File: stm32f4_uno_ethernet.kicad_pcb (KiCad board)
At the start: 2 copper layers, 68.6 x 53.3 mm, 57 parts, among them J104 STM32 GPIO, J106 Power, J107 Ethernet, J110 Analog, J111 Conn_01x04, J201 RJ45-TH_B-1-1, U201 SRV05-4, U202 LAN8742A, Y201 25MHz

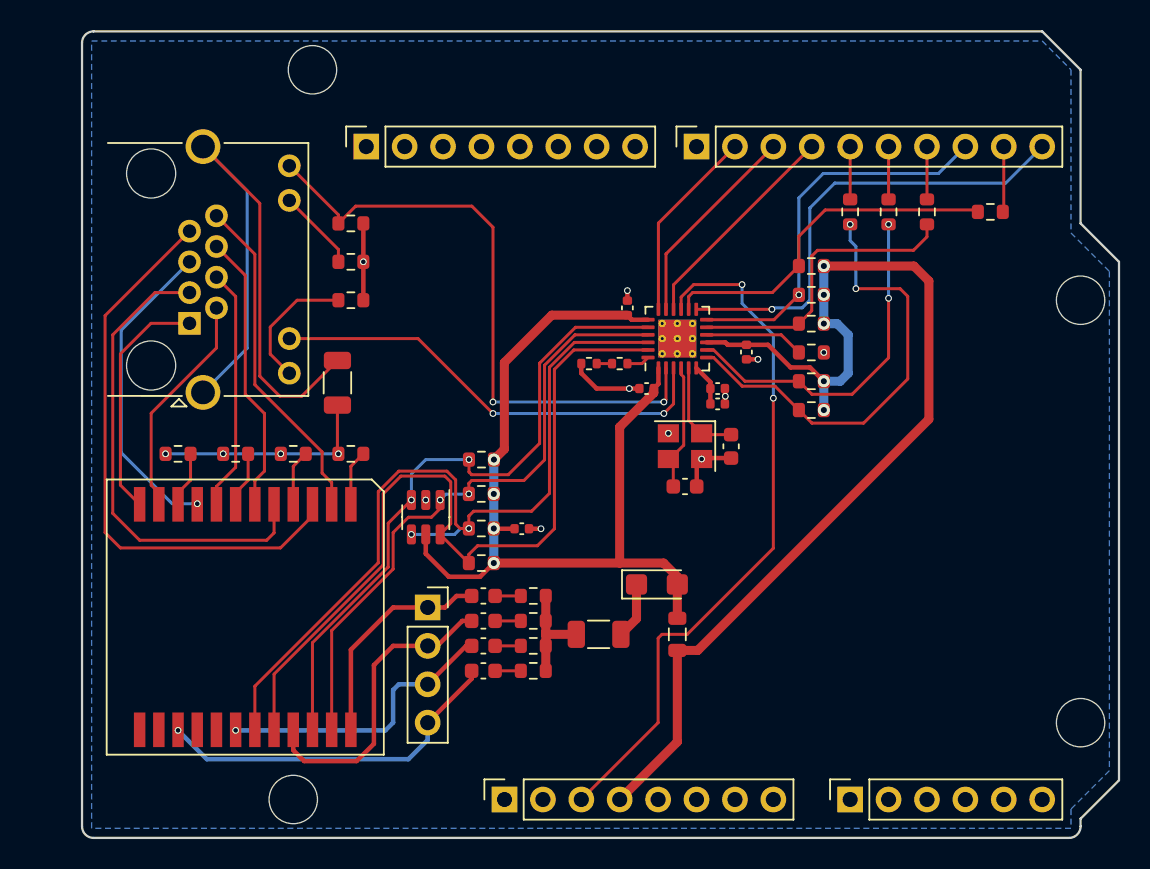
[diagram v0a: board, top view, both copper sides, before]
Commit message: Replace transformer, replace RJ45 3D model
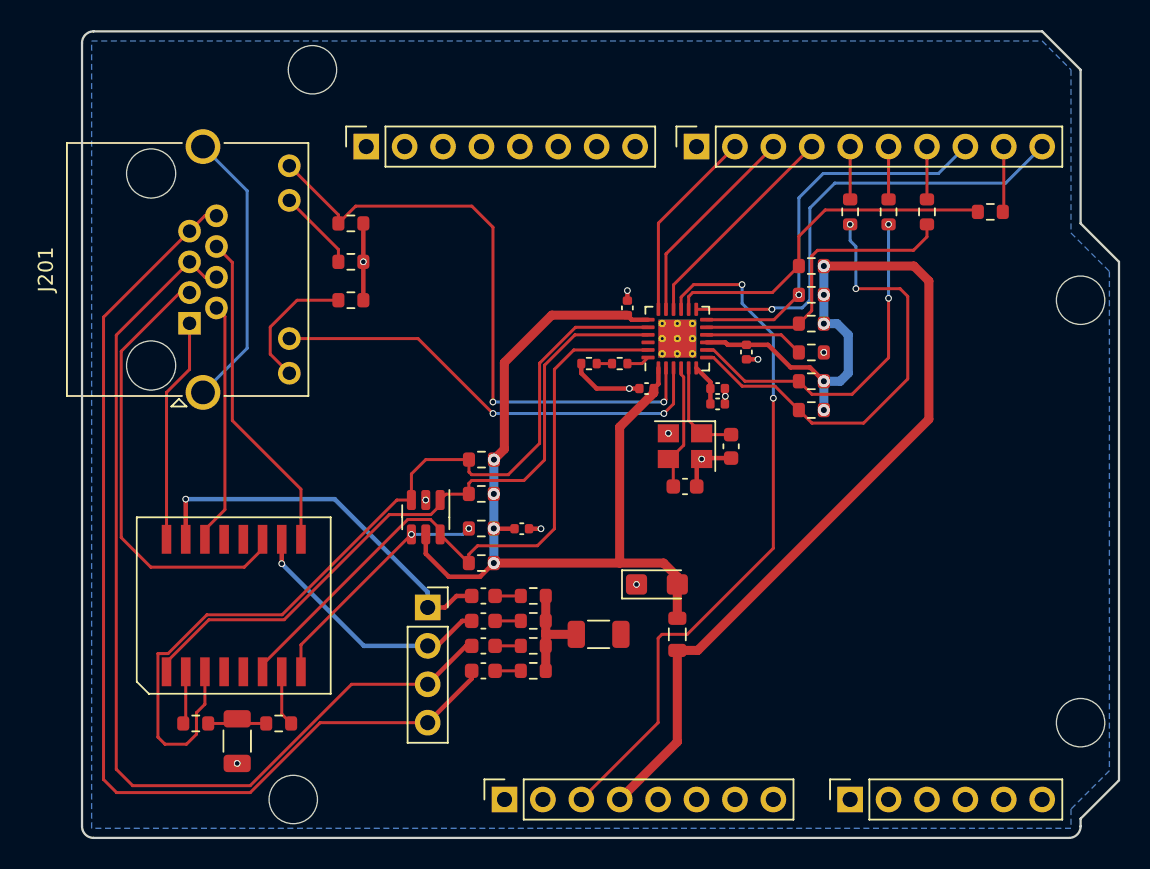
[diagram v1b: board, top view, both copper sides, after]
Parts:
- removed R218, R221: 75, Resistor_SMD:R_0603_1608Metric
- J201: footprint Project_Library:RJ45-TH_B-1-1 -> Project_Library:Boomele RJ45-TH_B-1-1
- TR201: value G2474CG -> YDS-Tech 11FB-05NL; footprint Project_Library:Mentech G2474CG 24pin 17.2mmx13.97mm -> Project_Library:YDS-Tech 11FB-05NL
- moved C208 24.6 mm to (110.3, 93.6), turned to -90 degrees
- moved R205 20.6 mm to (107.5, 92.4), turned to 180 degrees
- moved R213 17.9 mm to (113.0, 92.4)
- moved TR201 10.2 mm to (110.0, 84.6), turned to 0 degrees
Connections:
- C208 pad 2: Earth -> GND
- C213 pad 1: /Ethernet/PR45 -> /Ethernet/LAN4
- C214 pad 1: /Ethernet/PR78 -> /Ethernet/LAN7
- C215 pad 2: GND -> Earth
- J111 pad 3: /Ethernet/PR45 -> /Ethernet/LAN4
- J111 pad 4: /Ethernet/PR78 -> /Ethernet/LAN7
- J201 pad 5: /Ethernet/LAN5 -> /Ethernet/LAN4
- J201 pad 8: /Ethernet/LAN8 -> /Ethernet/LAN7
- R205 pad 2: Net-(R205-Pad2) -> Net-(TR201-C_TX)
- R213 pad 2: Net-(R213-Pad2) -> Net-(TR201-C_RX)
- TR201 pad 1: Net-(R205-Pad2) -> /Ethernet/TX+
- TR201 pad 10: Net-(R221-Pad2) -> /Ethernet/PR36
- TR201 pad 11: /Ethernet/LAN2 -> /Ethernet/LAN3
- TR201 pad 12: /Ethernet/LAN1 -> unconnected-(TR201-NC-Pad12)
- TR201 pad 14: unconnected-(TR201-MX4+-Pad14) -> /Ethernet/LAN2
- TR201 pad 15: /Ethernet/PR78 -> /Ethernet/PR12
- TR201 pad 16: unconnected-(TR201-MX3--Pad16) -> /Ethernet/LAN1
- TR201 pad 2: /Ethernet/LAN8 -> Net-(TR201-C_TX)
- TR201 pad 3: /Ethernet/LAN7 -> /Ethernet/TX-
- TR201 pad 4: Net-(R213-Pad2) -> unconnected-(TR201-NC-Pad4)
- TR201 pad 5: /Ethernet/LAN3 -> unconnected-(TR201-NC-Pad5)
- TR201 pad 6: /Ethernet/LAN6 -> /Ethernet/RX+
- TR201 pad 7: Net-(R218-Pad2) -> Net-(TR201-C_RX)
- TR201 pad 8: /Ethernet/LAN4 -> /Ethernet/RX-
- TR201 pad 9: /Ethernet/LAN5 -> /Ethernet/LAN6
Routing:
- net /Ethernet/LAN4: track 16.1 -> 65.5 mm
- net /Ethernet/RX-: track 55.2 -> 16.1 mm
- net /Ethernet/LAN7: track 38.0 -> 69.2 mm
- net /Ethernet/PR78: track 23.6 -> 0.00 mm, vias 1 -> 0
- net Earth: track 42.1 -> 18.7 mm
- net /Ethernet/LAN8: track 22.2 -> 0.00 mm
- net /Ethernet/LAN5: track 21.0 -> 0.00 mm, vias 1 -> 0
- net /Ethernet/PR45: track 19.2 -> 0.00 mm, vias 1 -> 0
- net /Ethernet/TX-: track 43.7 -> 59.7 mm, vias 2 -> 0
- net /Ethernet/PR12: track 14.8 -> 25.4 mm, vias 0 -> 1
- net /Ethernet/RX+: track 54.6 -> 44.0 mm
- net Net-(C208-Pad1): track 14.7 -> 4.09 mm, vias 4 -> 0
- net /Ethernet/TX+: track 41.4 -> 45.7 mm, vias 2 -> 0
- net GND: track 20.9 -> 17.2 mm, vias 10 -> 12
- net Net-(R221-Pad2): track 3.68 -> 0.00 mm
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
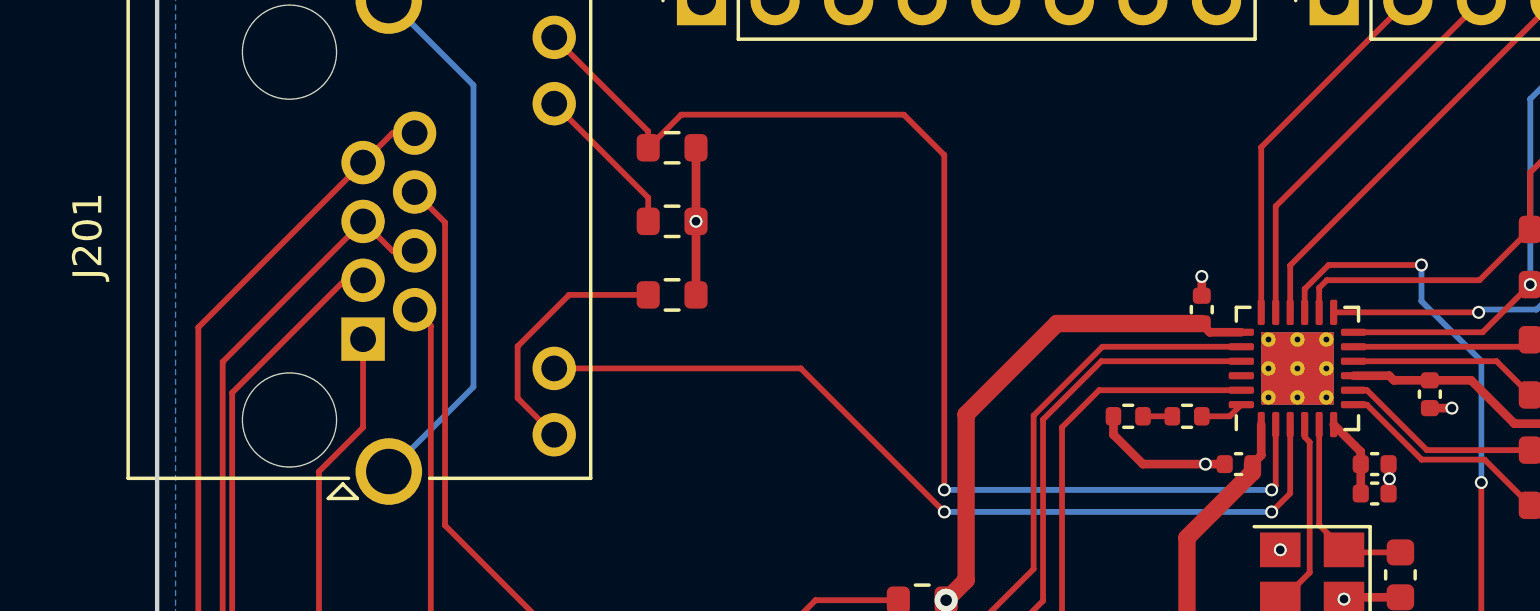
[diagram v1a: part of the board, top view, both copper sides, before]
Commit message: Change LAN footprint
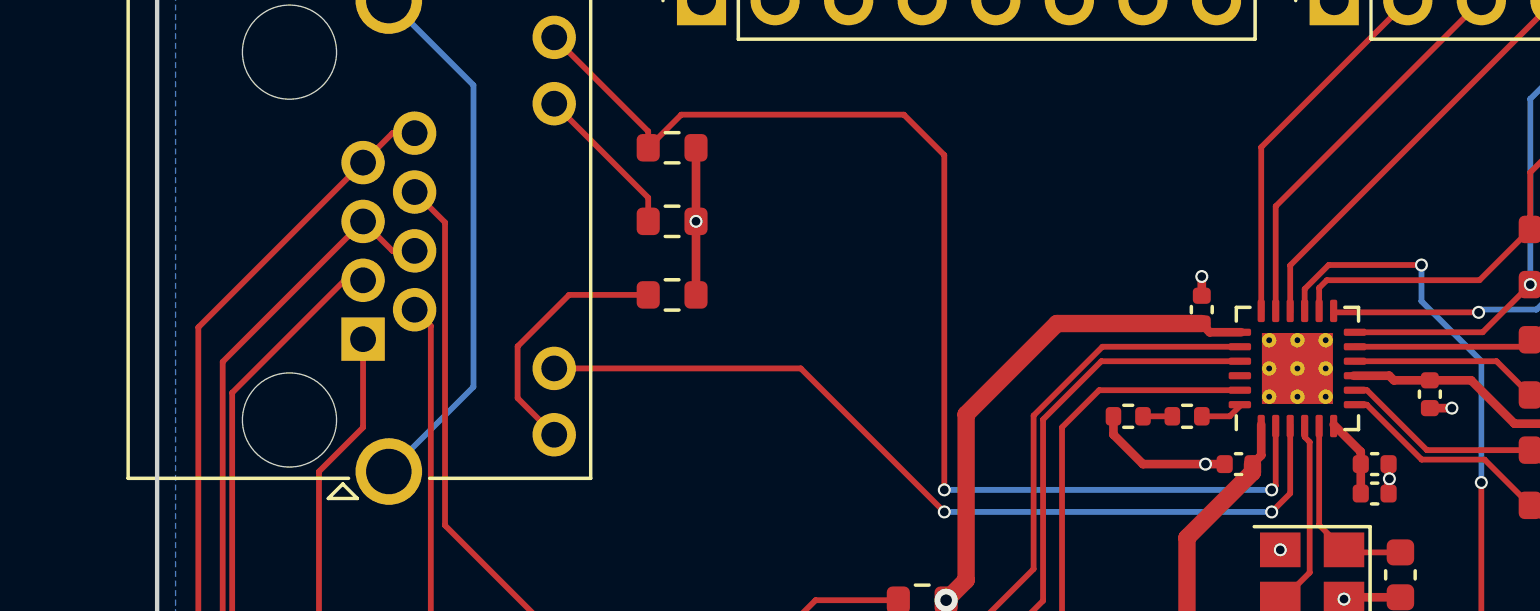
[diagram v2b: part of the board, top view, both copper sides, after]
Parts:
- U202: footprint Package_DFN_QFN:VQFN-24-1EP_4x4mm_P0.5mm_EP2.5x2.5mm_ThermalVias -> Package_DFN_QFN:VQFN-24-1EP_4x4mm_P0.5mm_EP2.45x2.45mm_ThermalVias

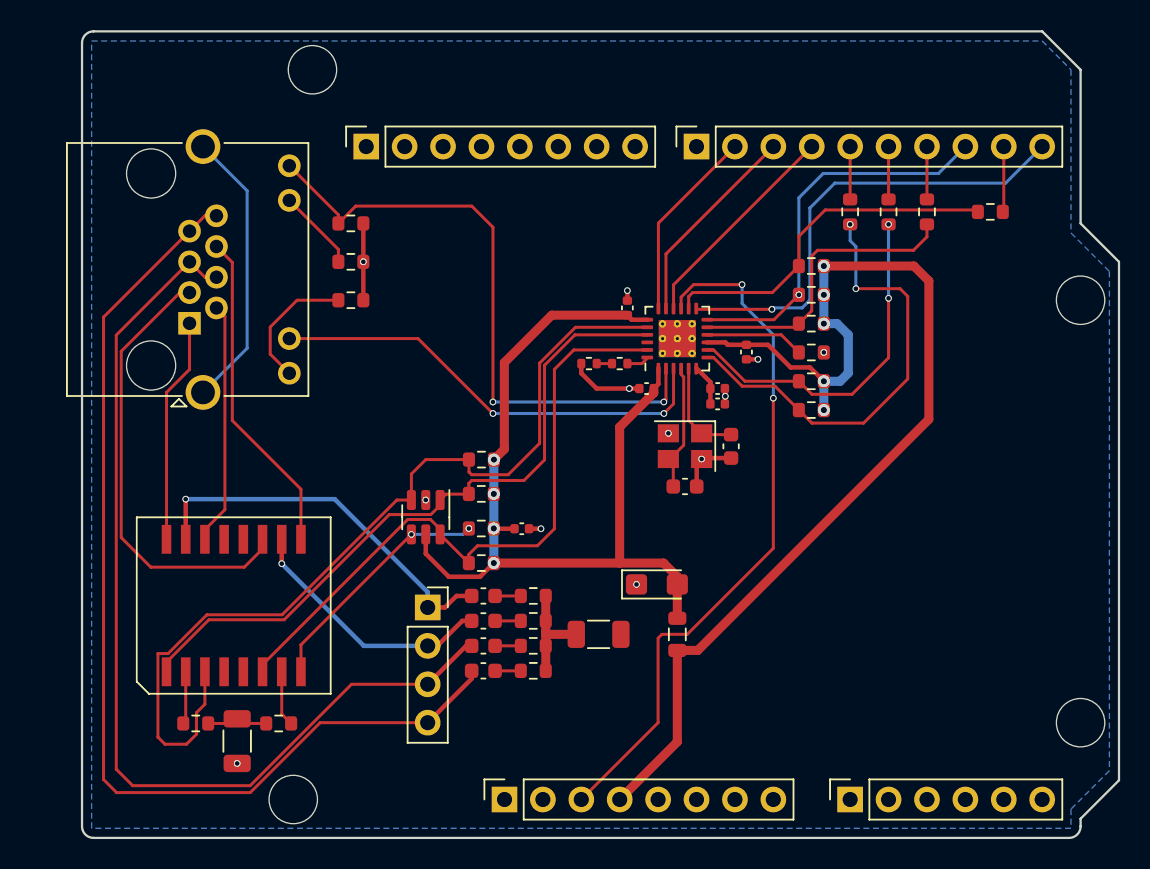
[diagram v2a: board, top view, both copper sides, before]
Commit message: Add ETH_RXER
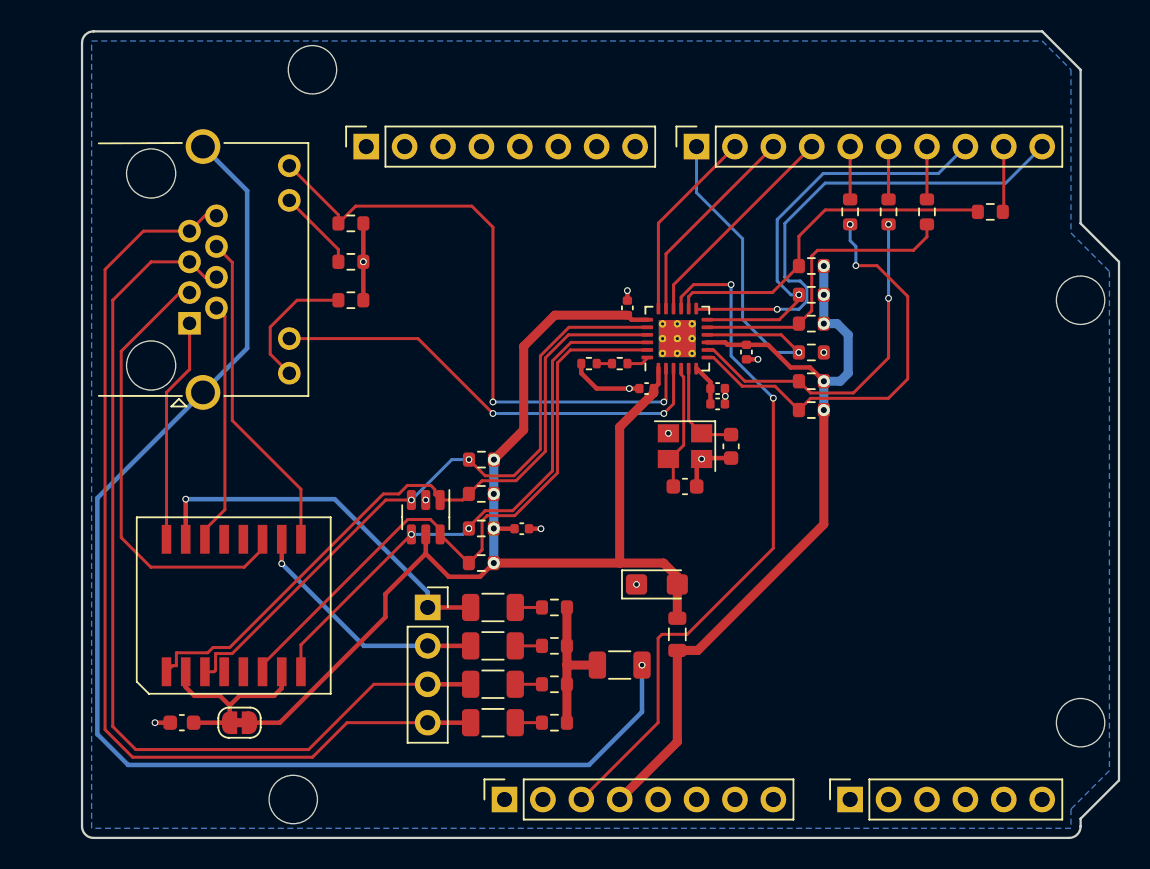
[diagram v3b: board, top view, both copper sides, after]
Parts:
- removed C208: 1n 2kV, Capacitor_SMD:C_1206_3216Metric
- removed R205, R213: 75, Resistor_SMD:R_0603_1608Metric
- added C217: 22n 50V, Capacitor_SMD:C_0603_1608Metric, F.Cu at (106.6, 92.4)
- added JP201: 3V3->VDD_ETH, Jumper:SolderJumper-2_P1.3mm_Bridged_RoundedPad1.0x1.5mm, F.Cu at (110.4, 92.4)
- C211, C212, C213, C214: value 100n 100V -> 1n 2kV; footprint Capacitor_SMD:C_0603_1608Metric -> Capacitor_SMD:C_1206_3216Metric
- moved R227 3.70 mm to (131.2, 92.4)
- moved C214 3.49 mm to (127.2, 92.4)
- moved R226 2.90 mm to (131.2, 89.8)
- moved C213 2.62 mm to (127.2, 89.8)
- moved C215 2.47 mm to (135.6, 88.6)
- moved R225 2.16 mm to (131.2, 87.3)
- moved C212 1.77 mm to (127.2, 87.3)
- moved R224 1.59 mm to (131.2, 84.8)
- moved C211 0.99 mm to (127.2, 84.8)
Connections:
- net /Ethernet/LAN4 renamed /Ethernet/PR45
- net /Ethernet/LAN7 renamed /Ethernet/PR78
- J104 pad 1: /PB14 -> GND
- J107 pad 1: GND -> /ETH_RXER
- R214 pad 1: /Ethernet/RXER -> /ETH_RXER
- TR201 pad 2: Net-(TR201-C_TX) -> /Ethernet/VDD_ETH
- TR201 pad 7: Net-(TR201-C_RX) -> /Ethernet/VDD_ETH
- U202 pad 10: /Ethernet/RXER -> /ETH_RXER
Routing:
- net Earth: track 18.7 -> 85.6 mm, vias 0 -> 1
- net /ETH_RXER: track 0.00 -> 23.9 mm, vias 0 -> 1
- net /Ethernet/RX-: track 16.1 -> 37.3 mm
- net +3V3: track 71.7 -> 53.0 mm
- net /Ethernet/VDDxA: track 61.9 -> 79.0 mm
- net /Ethernet/TX-: track 59.7 -> 43.8 mm, vias 0 -> 2
- net /Ethernet/VDD_ETH: track 0.00 -> 12.9 mm
- net /Ethernet/RXER: track 6.58 -> 0.00 mm
- net Net-(C208-Pad1): track 4.09 -> 0.00 mm
- net /Ethernet/PR78: track 69.2 -> 65.2 mm
- net Net-(TR201-C_RX): track 3.68 -> 0.00 mm
- net Net-(TR201-C_TX): track 3.49 -> 0.00 mm
- net /Ethernet/PR45: track 65.5 -> 62.6 mm
- net Net-(C215-Pad1): track 6.97 -> 9.64 mm
- net /ETH_MDC: track 30.9 -> 32.9 mm
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
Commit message: Set DNP
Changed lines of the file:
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@@
     (fp_line (start 1.6 0.8) (end -1.6 0.8)
       (stroke (width 0.1) (type solid)) (layer "F.Fab"))
-    (pad "1" smd roundrect (at -1.475 0) (size 1.15 1.8) (layers "F.Cu" "F.Paste" "F.Mask") (roundrect_rratio 0.217391)
+    (pad "1" smd roundrect (at -1.475 0) (size 1.15 1.8) (layers "F.Cu" "F.Paste" "F.Mask") (roundrect_rratio 0.2173913043)
       (net 23 "/Ethernet/PR45") (pintype "passive"))
-    (pad "2" smd roundrect (at 1.475 0) (size 1.15 1.8) (layers "F.Cu" "F.Paste" "F.Mask") (roundrect_rratio 0.217391)
+    (pad "2" smd roundrect (at 1.475 0) (size 1.15 1.8) (layers "F.Cu" "F.Paste" "F.Mask") (roundrect_rratio 0.2173913043)
       (net 33 "Net-(C213-Pad2)") (pintype "passive"))
     (model "${KICAD6_3DMODEL_DIR}/Capacitor_SMD.3dshapes/C_1206_3216Metric.wrl"
@@
     (fp_line (start 1.6 0.8) (end -1.6 0.8)
       (stroke (width 0.1) (type solid)) (layer "F.Fab"))
-    (pad "1" smd roundrect (at -1.475 0) (size 1.15 1.8) (layers "F.Cu" "F.Paste" "F.Mask") (roundrect_rratio 0.217391)
+    (pad "1" smd roundrect (at -1.475 0) (size 1.15 1.8) (layers "F.Cu" "F.Paste" "F.Mask") (roundrect_rratio 0.2173913043)
       (net 31 "/Ethernet/PR36") (pintype "passive"))
-    (pad "2" smd roundrect (at 1.475 0) (size 1.15 1.8) (layers "F.Cu" "F.Paste" "F.Mask") (roundrect_rratio 0.217391)
+    (pad "2" smd roundrect (at 1.475 0) (size 1.15 1.8) (layers "F.Cu" "F.Paste" "F.Mask") (roundrect_rratio 0.2173913043)
       (net 32 "Net-(C212-Pad2)") (pintype "passive"))
     (model "${KICAD6_3DMODEL_DIR}/Capacitor_SMD.3dshapes/C_1206_3216Metric.wrl"
@@
     (fp_line (start 1.6 0.8) (end -1.6 0.8)
       (stroke (width 0.1) (type solid)) (layer "F.Fab"))
-    (pad "1" smd roundrect (at -1.475 0) (size 1.15 1.8) (layers "F.Cu" "F.Paste" "F.Mask") (roundrect_rratio 0.217391)
+    (pad "1" smd roundrect (at -1.475 0) (size 1.15 1.8) (layers "F.Cu" "F.Paste" "F.Mask") (roundrect_rratio 0.2173913043)
       (net 35 "Net-(C215-Pad1)") (pintype "passive"))
-    (pad "2" smd roundrect (at 1.475 0) (size 1.15 1.8) (layers "F.Cu" "F.Paste" "F.Mask") (roundrect_rratio 0.217391)
+    (pad "2" smd roundrect (at 1.475 0) (size 1.15 1.8) (layers "F.Cu" "F.Paste" "F.Mask") (roundrect_rratio 0.2173913043)
       (net 62 "Earth") (pintype "passive"))
     (model "${KICAD6_3DMODEL_DIR}/Capacitor_SMD.3dshapes/C_1206_3216Metric.wrl"
@@
     (fp_line (start 1.6 0.8) (end -1.6 0.8)
       (stroke (width 0.1) (type solid)) (layer "F.Fab"))
-    (pad "1" smd roundrect (at -1.475 0) (size 1.15 1.8) (layers "F.Cu" "F.Paste" "F.Mask") (roundrect_rratio 0.217391)
+    (pad "1" smd roundrect (at -1.475 0) (size 1.15 1.8) (layers "F.Cu" "F.Paste" "F.Mask") (roundrect_rratio 0.2173913043)
       (net 29 "/Ethernet/PR12") (pintype "passive"))
-    (pad "2" smd roundrect (at 1.475 0) (size 1.15 1.8) (layers "F.Cu" "F.Paste" "F.Mask") (roundrect_rratio 0.217391)
+    (pad "2" smd roundrect (at 1.475 0) (size 1.15 1.8) (layers "F.Cu" "F.Paste" "F.Mask") (roundrect_rratio 0.2173913043)
       (net 30 "Net-(C211-Pad2)") (pintype "passive"))
     (model "${KICAD6_3DMODEL_DIR}/Capacitor_SMD.3dshapes/C_1206_3216Metric.wrl"
@@
     (fp_line (start 1.6 0.8) (end 1.6 -0.8)
       (stroke (width 0.1) (type solid)) (layer "F.Fab"))
-    (pad "1" smd roundrect (at -1.35 0) (size 1.4 1.35) (layers "F.Cu" "F.Paste" "F.Mask") (roundrect_rratio 0.185185)
+    (pad "1" smd roundrect (at -1.35 0) (size 1.4 1.35) (layers "F.Cu" "F.Paste" "F.Mask") (roundrect_rratio 0.1851851852)
       (net 1 "GND") (pintype "passive"))
-    (pad "2" smd roundrect (at 1.35 0) (size 1.4 1.35) (layers "F.Cu" "F.Paste" "F.Mask") (roundrect_rratio 0.185185)
+    (pad "2" smd roundrect (at 1.35 0) (size 1.4 1.35) (layers "F.Cu" "F.Paste" "F.Mask") (roundrect_rratio 0.1851851852)
       (net 52 "/Ethernet/VDDxA") (pintype "passive"))
     (model "${KICAD6_3DMODEL_DIR}/Capacitor_Tantalum_SMD.3dshapes/CP_EIA-3216-18_Kemet-A.wrl"
@@
     (fp_line (start 1.6 0.8) (end -1.6 0.8)
       (stroke (width 0.1) (type solid)) (layer "F.Fab"))
-    (pad "1" smd roundrect (at -1.475 0) (size 1.15 1.8) (layers "F.Cu" "F.Paste" "F.Mask") (roundrect_rratio 0.217391)
+    (pad "1" smd roundrect (at -1.475 0) (size 1.15 1.8) (layers "F.Cu" "F.Paste" "F.Mask") (roundrect_rratio 0.2173913043)
       (net 28 "/Ethernet/PR78") (pintype "passive"))
-    (pad "2" smd roundrect (at 1.475 0) (size 1.15 1.8) (layers "F.Cu" "F.Paste" "F.Mask") (roundrect_rratio 0.217391)
+    (pad "2" smd roundrect (at 1.475 0) (size 1.15 1.8) (layers "F.Cu" "F.Paste" "F.Mask") (roundrect_rratio 0.2173913043)
       (net 34 "Net-(C214-Pad2)") (pintype "passive"))
     (model "${KICAD6_3DMODEL_DIR}/Capacitor_SMD.3dshapes/C_1206_3216Metric.wrl"

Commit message: #1 Use new central library KiCad-Lib
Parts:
- J201: footprint Project_Library:Boomele RJ45-TH_B-1-1 -> #Connector:Boomele RJ45-TH_B-1-1
- TR201: footprint Project_Library:YDS-Tech 11FB-05NL -> #Transformer:YDS-Tech 11FB-05NL
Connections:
- net Net-(J201-Pad11) renamed /Ethernet/LED2_K
- net Net-(J201-Pad9) renamed /Ethernet/LED1_K
